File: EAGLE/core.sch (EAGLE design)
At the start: 47 parts, among them IC1 MCP1825S-3302E, Q1 MMDT3904, U2 STM32F10XCXT6, U3 SST25VF040B-S2, X1 USB-MICROB, X2 IPEX-20279-001E, Y1 32Khz, Y2 8Mhz

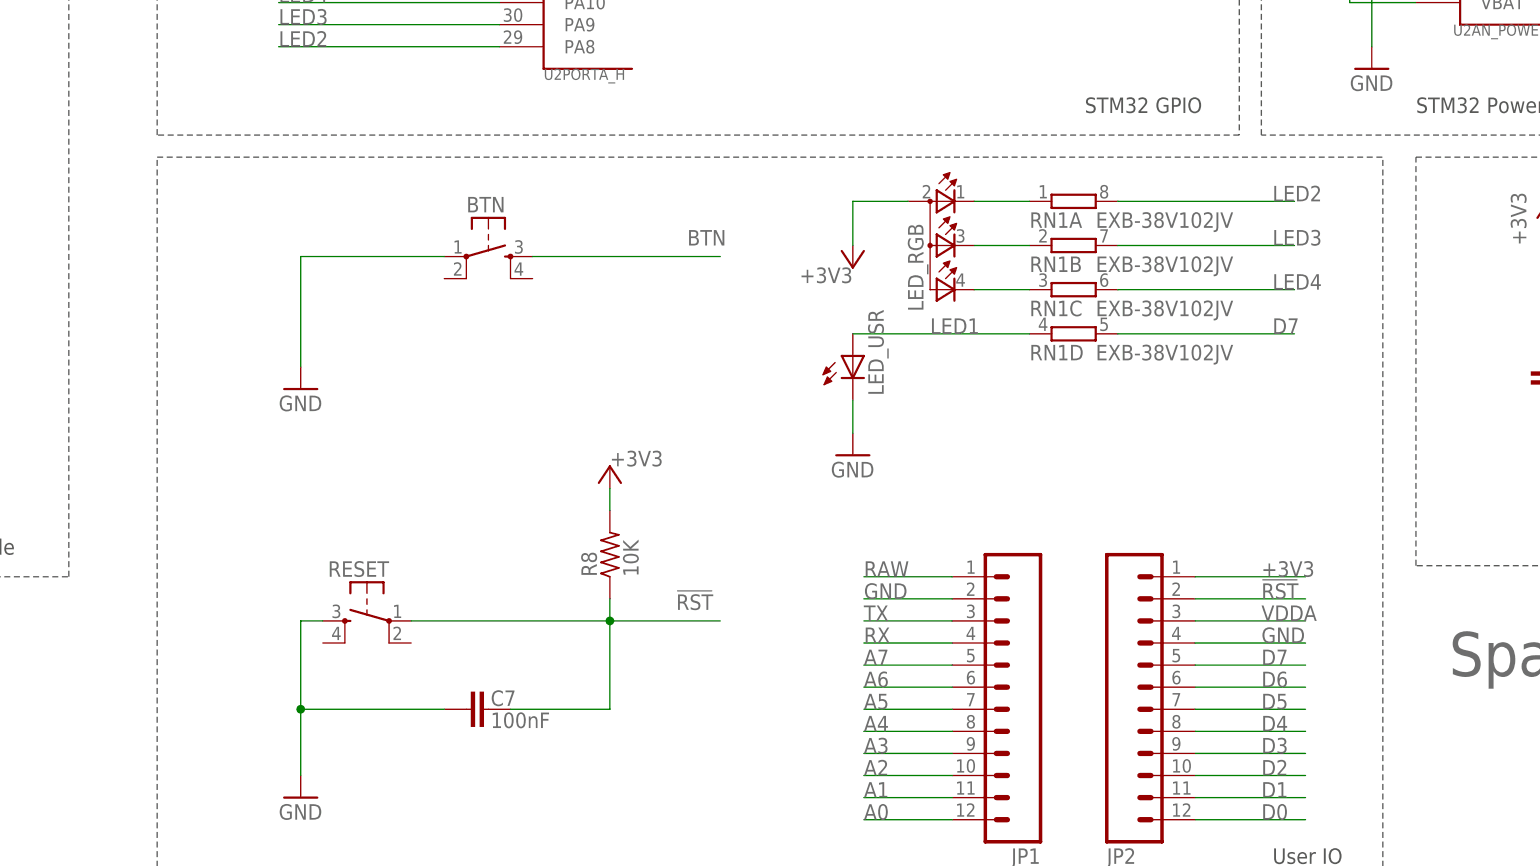
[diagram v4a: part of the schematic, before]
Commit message: Finished Schematic and PCB Layout
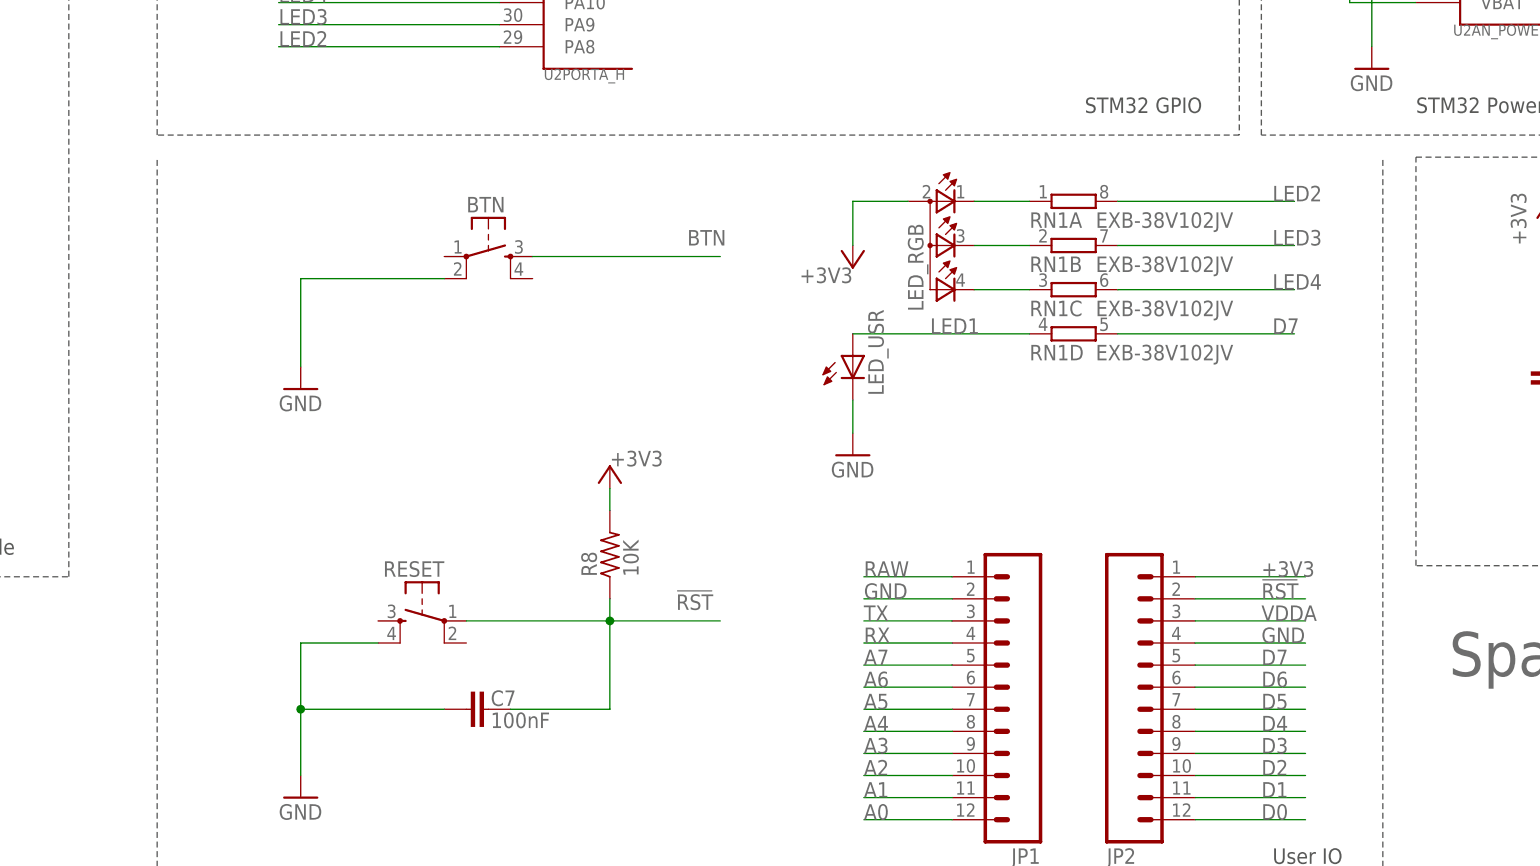
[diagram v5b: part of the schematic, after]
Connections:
- net GND: now also BTN.2, RESET.4; no longer BTN.1, RESET.3
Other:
- moved on the sheet: RESET
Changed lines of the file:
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@@
 <setting verticaltext="up"/>
 </settings>
-<grid distance="0.1" unitdist="inch" unit="inch" style="lines" multiple="1" display="no" altdistance="0.01" altunitdist="inch" altunit="inch"/>
+<grid distance="50" unitdist="mil" unit="mil" style="lines" multiple="1" display="yes" altdistance="0.01" altunitdist="inch" altunit="inch"/>
 <layers>
 <layer number="1" name="Top" color="4" fill="1" visible="no" active="no"/>
@@
 <layer number="91" name="Nets" color="2" fill="1" visible="yes" active="yes"/>
 <layer number="92" name="Busses" color="1" fill="1" visible="yes" active="yes"/>
-<layer number="93" name="Pins" color="2" fill="1" visible="no" active="yes"/>
+<layer number="93" name="Pins" color="2" fill="1" visible="yes" active="yes"/>
 <layer number="94" name="Symbols" color="4" fill="1" visible="yes" active="yes"/>
 <layer number="95" name="Names" color="7" fill="1" visible="yes" active="yes"/>
@@
 <text x="477.52" y="40.64" size="1.778" layer="97">External FLASH</text>
 <wire x1="256.54" y1="2.54" x2="256.54" y2="86.36" width="0.1524" layer="97" style="dashdot"/>
-<wire x1="256.54" y1="86.36" x2="397.51" y2="86.36" width="0.1524" layer="97" style="dashdot"/>
 <wire x1="397.51" y1="2.54" x2="397.51" y2="86.36" width="0.1524" layer="97" style="dashdot"/>
 <wire x1="256.54" y1="2.54" x2="397.51" y2="2.54" width="0.1524" layer="97" style="dashdot"/>
@@
 </instance>
 <instance part="U2" gate="RESET" x="436.88" y="170.18"/>
-<instance part="RESET" gate="S" x="280.67" y="33.02" smashed="yes" rot="MR0">
-<attribute name="NAME" x="283.21" y="38.1" size="1.778" layer="95" rot="MR0"/>
+<instance part="RESET" gate="S" x="287.02" y="33.02" smashed="yes" rot="MR0">
+<attribute name="NAME" x="289.56" y="38.1" size="1.778" layer="95" rot="MR0"/>
 </instance>
 <instance part="R8" gate="G$1" x="308.61" y="40.64" smashed="yes" rot="R90">
@@
 </segment>
 <segment>
-<pinref part="GND13" gate="1" pin="GND"/>
-<wire x1="273.05" y1="74.93" x2="273.05" y2="62.23" width="0.1524" layer="91"/>
-<pinref part="BTN" gate="S" pin="1"/>
-<wire x1="289.56" y1="74.93" x2="273.05" y2="74.93" width="0.1524" layer="91"/>
-</segment>
-<segment>
 <pinref part="U3" gate="A" pin="VSS"/>
 <wire x1="457.2" y1="55.88" x2="444.5" y2="55.88" width="0.1524" layer="91"/>
@@
 <pinref part="GND12" gate="1" pin="GND"/>
 <wire x1="273.05" y1="22.86" x2="273.05" y2="15.24" width="0.1524" layer="91"/>
-<pinref part="RESET" gate="S" pin="3"/>
-<wire x1="275.59" y1="33.02" x2="273.05" y2="33.02" width="0.1524" layer="91"/>
-<wire x1="273.05" y1="33.02" x2="273.05" y2="22.86" width="0.1524" layer="91"/>
+<pinref part="RESET" gate="S" pin="4"/>
+<wire x1="281.94" y1="30.48" x2="273.05" y2="30.48" width="0.1524" layer="91"/>
+<wire x1="273.05" y1="30.48" x2="273.05" y2="22.86" width="0.1524" layer="91"/>
 <junction x="273.05" y="22.86"/>
 </segment>
@@
 <pinref part="GND14" gate="1" pin="GND"/>
 <wire x1="488.95" y1="139.7" x2="488.95" y2="135.89" width="0.1524" layer="91"/>
+</segment>
+<segment>
+<pinref part="BTN" gate="S" pin="2"/>
+<pinref part="GND13" gate="1" pin="GND"/>
+<wire x1="289.56" y1="72.39" x2="273.05" y2="72.39" width="0.1524" layer="91"/>
+<wire x1="273.05" y1="72.39" x2="273.05" y2="62.23" width="0.1524" layer="91"/>
 </segment>
 </net>
@@
 <wire x1="308.61" y1="33.02" x2="321.31" y2="33.02" width="0.1524" layer="91"/>
 <pinref part="RESET" gate="S" pin="1"/>
-<wire x1="285.75" y1="33.02" x2="308.61" y2="33.02" width="0.1524" layer="91"/>
-</segment>
-<segment>
+<wire x1="292.1" y1="33.02" x2="308.61" y2="33.02" width="0.1524" layer="91"/>
+</segment>
+<segment>

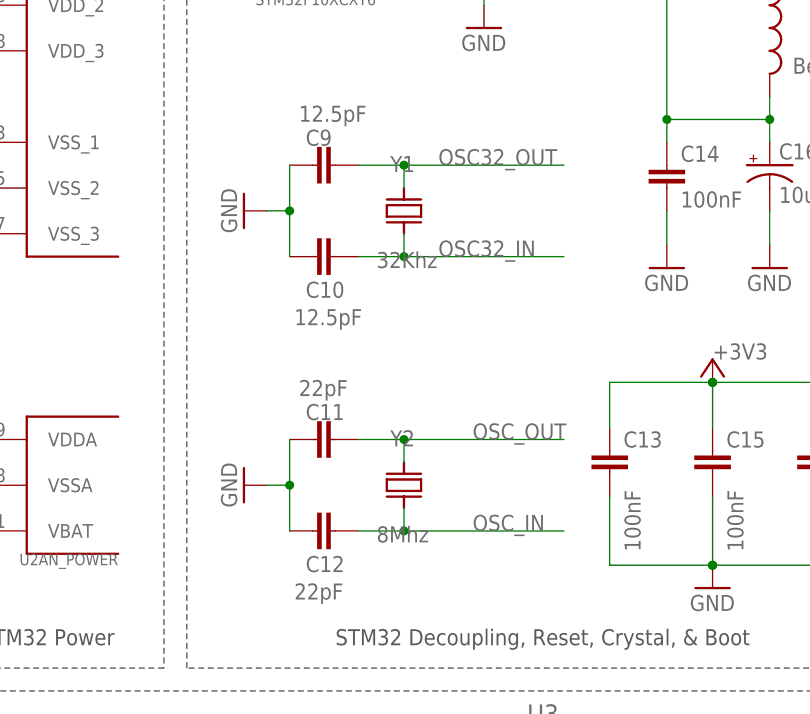
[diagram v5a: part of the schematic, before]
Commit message: Updated Crystal Section
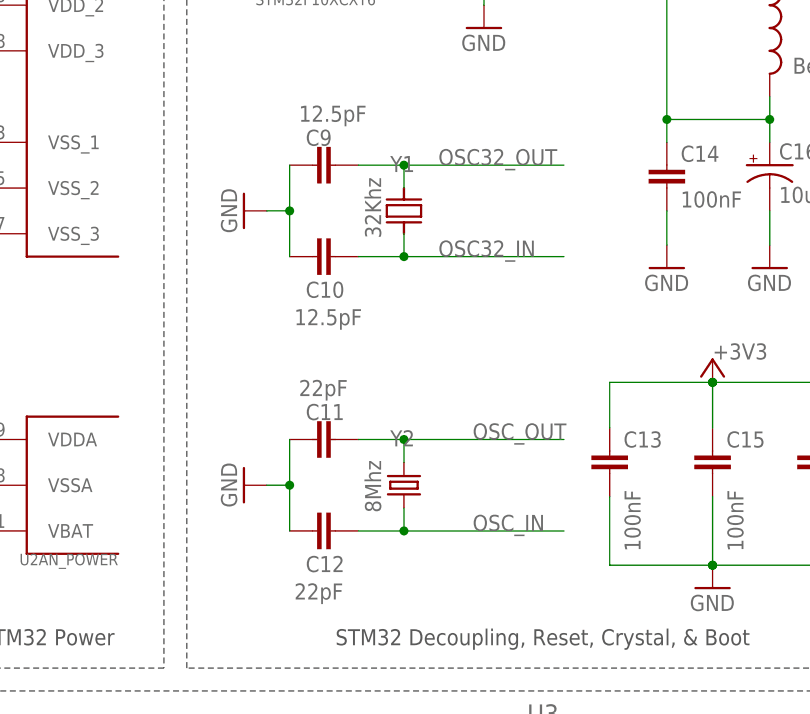
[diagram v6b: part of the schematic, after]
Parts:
- Y2: device Spark:Q_3.2X2.5 -> SparkFun-FreqCtrl:CRYSTAL5X3
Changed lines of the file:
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@@
 <layer number="91" name="Nets" color="2" fill="1" visible="yes" active="yes"/>
 <layer number="92" name="Busses" color="1" fill="1" visible="yes" active="yes"/>
-<layer number="93" name="Pins" color="2" fill="1" visible="yes" active="yes"/>
+<layer number="93" name="Pins" color="2" fill="1" visible="no" active="yes"/>
 <layer number="94" name="Symbols" color="4" fill="1" visible="yes" active="yes"/>
 <layer number="95" name="Names" color="7" fill="1" visible="yes" active="yes"/>
@@
 <part name="JP2" library="SparkFun" deviceset="M12" device="PTH" value=""/>
 <part name="GND4" library="SparkFun" deviceset="GND" device=""/>
-<part name="Y2" library="Spark" deviceset="Q" device="_3.2X2.5" value="8Mhz"/>
+<part name="Y2" library="SparkFun-FreqCtrl" deviceset="CRYSTAL" device="5X3" value="8Mhz"/>
 <part name="C11" library="rcl" deviceset="C-EU" device="C0603" value="22pF"/>
 <part name="C12" library="rcl" deviceset="C-EU" device="C0603" value="22pF"/>
@@
 <instance part="Y2" gate="G$1" x="448.31" y="109.22" smashed="yes" rot="R90">
 <attribute name="NAME" x="446.786" y="113.538" size="1.778" layer="95"/>
-<attribute name="VALUE" x="445.262" y="102.87" size="1.778" layer="96"/>
+<attribute name="VALUE" x="445.77" y="106.172" size="1.778" layer="96" rot="R90"/>
 </instance>
 <instance part="C11" gate="G$1" x="440.69" y="114.3" smashed="yes" rot="R270">
@@
 <instance part="Y1" gate="G$1" x="448.31" y="139.7" smashed="yes" rot="R90">
 <attribute name="NAME" x="446.786" y="144.018" size="1.778" layer="95"/>
-<attribute name="VALUE" x="445.262" y="133.35" size="1.778" layer="96"/>
+<attribute name="VALUE" x="445.77" y="136.652" size="1.778" layer="96" rot="R90"/>
 </instance>
 <instance part="C9" gate="G$1" x="440.69" y="144.78" smashed="yes" rot="R270">
@@
 <pinref part="C11" gate="G$1" pin="1"/>
 <wire x1="443.23" y1="114.3" x2="448.31" y2="114.3" width="0.1524" layer="91"/>
+<label x="455.93" y="114.3" size="1.778" layer="95"/>
 <pinref part="Y2" gate="G$1" pin="2"/>
 <wire x1="448.31" y1="114.3" x2="466.09" y2="114.3" width="0.1524" layer="91"/>
 <wire x1="448.31" y1="111.76" x2="448.31" y2="114.3" width="0.1524" layer="91"/>
 <junction x="448.31" y="114.3"/>
-<label x="455.93" y="114.3" size="1.778" layer="95"/>
 </segment>
 </net>
@@
 <pinref part="C12" gate="G$1" pin="1"/>
 <wire x1="443.23" y1="104.14" x2="448.31" y2="104.14" width="0.1524" layer="91"/>
+<label x="455.93" y="104.14" size="1.778" layer="95"/>
 <pinref part="Y2" gate="G$1" pin="1"/>
 <wire x1="448.31" y1="104.14" x2="466.09" y2="104.14" width="0.1524" layer="91"/>
 <wire x1="448.31" y1="106.68" x2="448.31" y2="104.14" width="0.1524" layer="91"/>
 <junction x="448.31" y="104.14"/>
-<label x="455.93" y="104.14" size="1.778" layer="95"/>
-</segment>
-</net>
+</segment>
+</net>

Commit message: Updated USB Section
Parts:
- X1: device Spark:USBUSB-MICROB-ALIGN -> Spark:USBUSB-MICROB-SMT-DIP
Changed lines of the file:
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@@
 <part name="R5" library="rcl" deviceset="R-US_" device="R0603" value="22"/>
 <part name="R6" library="rcl" deviceset="R-US_" device="R0603" value="22"/>
-<part name="X1" library="Spark" deviceset="USB" device="USB-MICROB-ALIGN" value="USB-MICROB"/>
+<part name="X1" library="Spark" deviceset="USB" device="USB-MICROB-SMT-DIP" value="USB-MICROB"/>
 <part name="GND3" library="SparkFun" deviceset="GND" device=""/>
 <part name="D1" library="SparkFun" deviceset="DIODE" device="SOD"/>

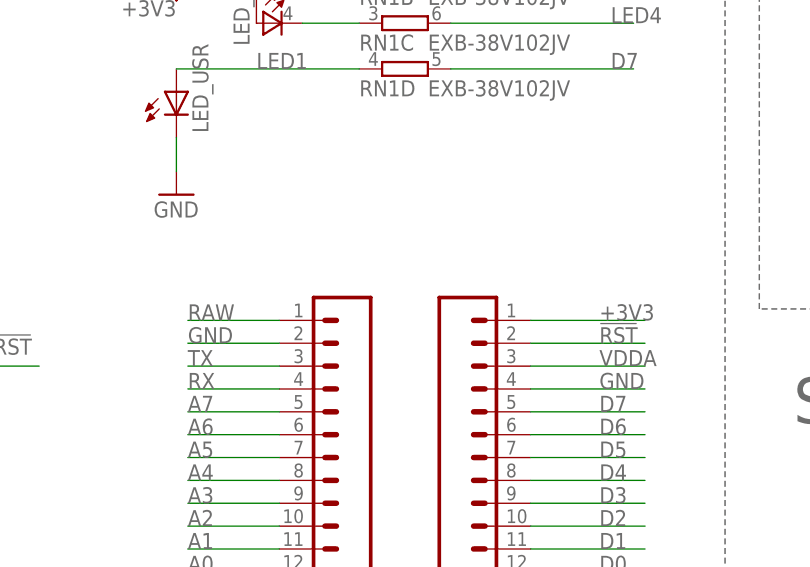
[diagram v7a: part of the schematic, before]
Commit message: Issue#22 modified and added the 1x12 pin header with smaller pads and holes to the spark library. Also modified the Core PCB with the updated header file issue#22 closed
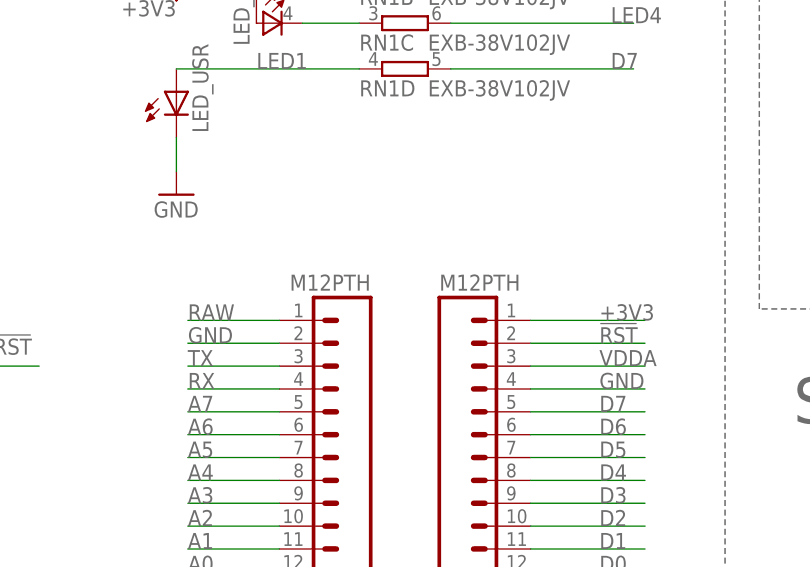
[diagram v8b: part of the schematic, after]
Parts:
- JP1, JP2: device SparkFun:M12PTH -> Spark:M12PTH
